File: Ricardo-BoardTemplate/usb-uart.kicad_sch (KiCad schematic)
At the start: 16 parts, among them J3 USB_C_Receptacle_USB2.0, U6 SC4216H/RT9059, U7 LTC4411

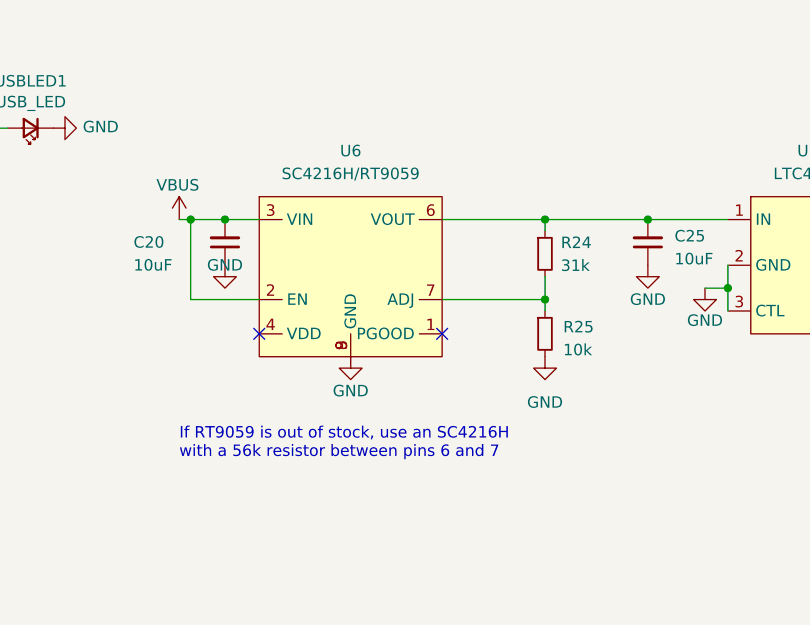
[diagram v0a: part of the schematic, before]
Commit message: most FP assignments to 0402
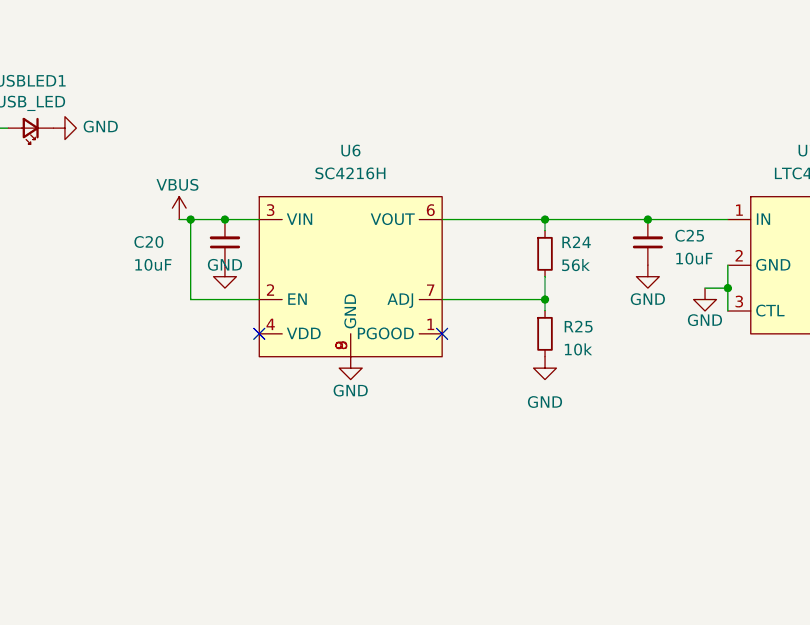
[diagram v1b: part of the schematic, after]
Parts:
- R15, R16, R18, R25: footprint Resistor_SMD:R_0603_1608Metric -> Resistor_SMD:R_0402_1005Metric
- R24: value 31k -> 56k; footprint Resistor_SMD:R_0603_1608Metric -> Resistor_SMD:R_0402_1005Metric
- U6: value SC4216H/RT9059 -> SC4216H
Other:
- note removed: "If RT9059 is out of stock, use an SC4216H with a 56k resistor between pins 6 and 7"
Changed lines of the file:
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@@
     (stroke (width 0) (type default) (color 0 0 0 0))
-  )
-  (text "If RT9059 is out of stock, use an SC4216H \nwith a 56k resistor between pins 6 and 7"
-    (at 179.07 129.54 0)
-    (effects (font (size 1.27 1.27)) (justify left bottom))
   )
   (label "Data+" (at 134.62 134.62 90)
@@
     (property "Reference" "R16" (id 0) (at 129.54 100.33 90))
     (property "Value" "5.1k" (id 1) (at 129.54 102.6414 90))
-    (property "Footprint" "Resistor_SMD:R_0603_1608Metric" (id 2) (at 123.19 99.06 0)
+    (property "Footprint" "Resistor_SMD:R_0402_1005Metric" (id 2) (at 123.19 99.06 0)
       (effects (font (size 1.27 1.27)) hide)
     )
@@
     (property "Reference" "R15" (id 0) (at 123.19 89.0016 90))
     (property "Value" "5.1k" (id 1) (at 123.19 91.313 90))
-    (property "Footprint" "Resistor_SMD:R_0603_1608Metric" (id 2) (at 123.19 93.98 0)
+    (property "Footprint" "Resistor_SMD:R_0402_1005Metric" (id 2) (at 123.19 93.98 0)
       (effects (font (size 1.27 1.27)) hide)
     )
@@
     (property "Reference" "R18" (id 0) (at 154.94 97.6884 90))
     (property "Value" "470" (id 1) (at 154.94 95.377 90))
-    (property "Footprint" "Resistor_SMD:R_0603_1608Metric" (id 2) (at 154.94 92.71 0)
+    (property "Footprint" "Resistor_SMD:R_0402_1005Metric" (id 2) (at 154.94 92.71 0)
       (effects (font (size 1.27 1.27)) hide)
     )
@@
       (effects (font (size 1.27 1.27)) (justify left))
     )
-    (property "Footprint" "Resistor_SMD:R_0603_1608Metric" (id 2) (at 219.71 115.57 0)
+    (property "Footprint" "Resistor_SMD:R_0402_1005Metric" (id 2) (at 219.71 115.57 0)
       (effects (font (size 1.27 1.27)) hide)
     )
@@
       (effects (font (size 1.27 1.27)) (justify left))
     )
-    (property "Value" "31k" (id 1) (at 221.4667 107.9905 0)
-      (effects (font (size 1.27 1.27)) (justify left))
-    )
-    (property "Footprint" "Resistor_SMD:R_0603_1608Metric" (id 2) (at 219.71 106.68 0)
+    (property "Value" "56k" (id 1) (at 221.4667 107.9905 0)
+      (effects (font (size 1.27 1.27)) (justify left))
+    )
+    (property "Footprint" "Resistor_SMD:R_0402_1005Metric" (id 2) (at 219.71 106.68 0)
       (effects (font (size 1.27 1.27)) hide)
     )
@@
     (in_bom yes) (on_board yes) (fields_autoplaced)
     (property "Reference" "U6" (id 0) (at 198.12 95.25 0))
-    (property "Value" "SC4216H/RT9059" (id 1) (at 198.12 97.79 0))
+    (property "Value" "SC4216H" (id 1) (at 198.12 97.79 0))
     (property "Footprint" "iclr:SOIC127P599X175-9N" (id 2) (at 198.12 96.52 0)
       (effects (font (size 1.27 1.27)) hide)

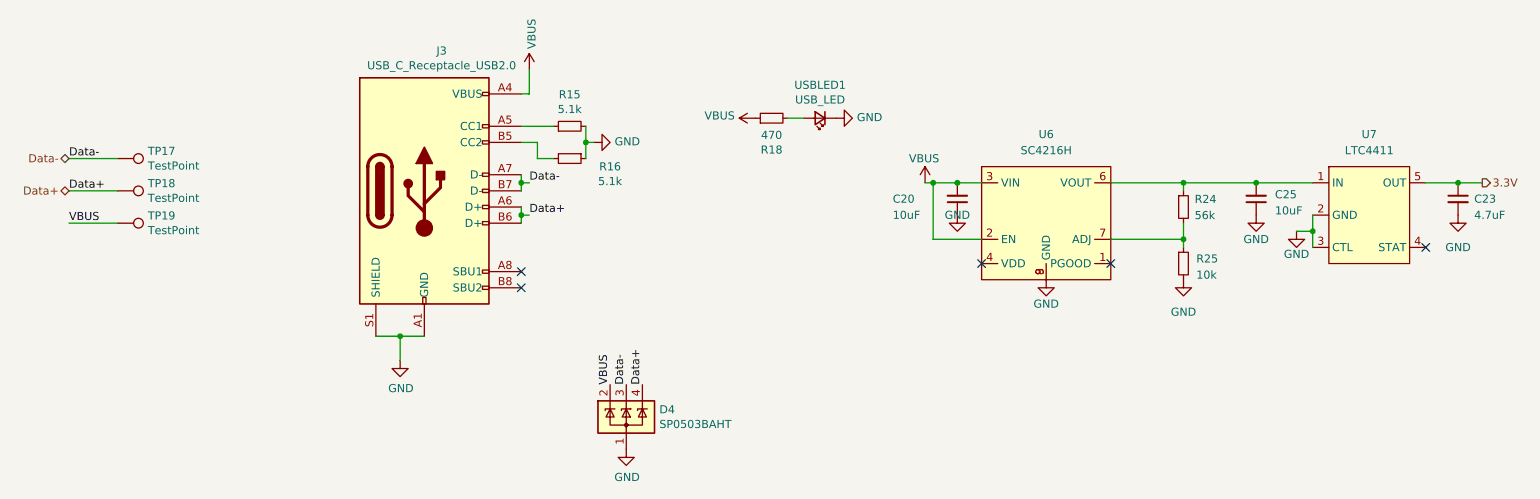
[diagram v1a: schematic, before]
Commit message: Initial buck boost layout
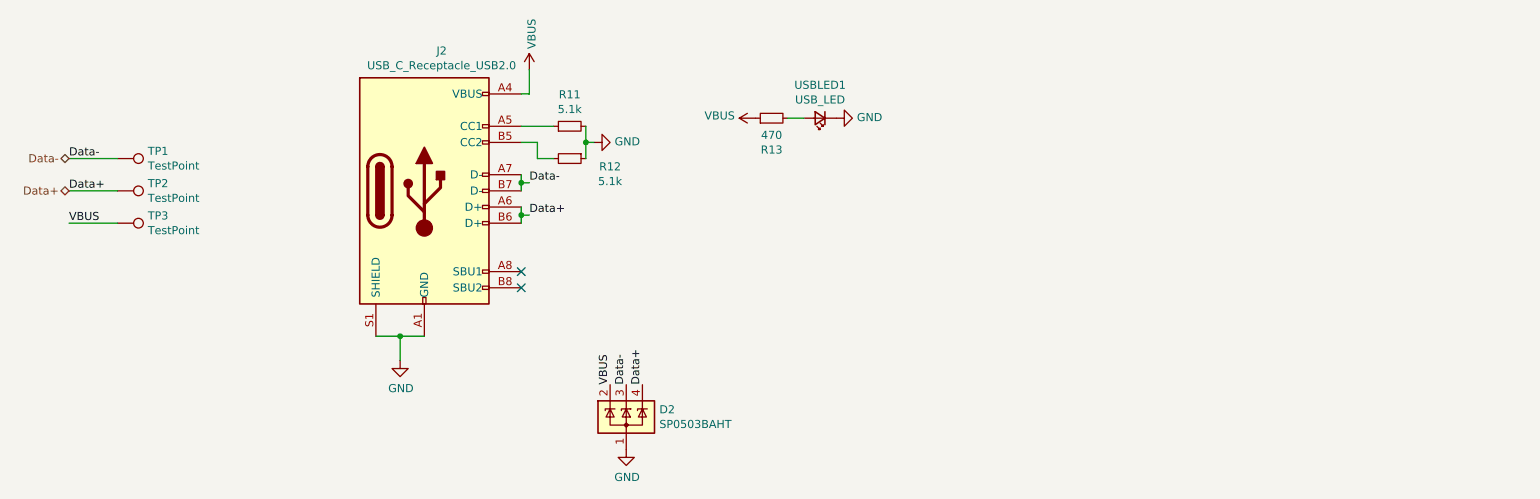
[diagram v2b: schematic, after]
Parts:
- removed C20, C25: 10uF, Capacitor_SMD:C_0603_1608Metric, symbol Device:C_Small
- removed C23: 4.7uF, Capacitor_SMD:C_0603_1608Metric, symbol Device:C_Small
- removed R24: 56k, Resistor_SMD:R_0402_1005Metric, symbol Device:R_Small
- removed R25: 10k, Resistor_SMD:R_0402_1005Metric, symbol Device:R_Small
- removed U6: SC4216H, iclr:SOIC127P599X175-9N, symbol iclr:RT9025-25GSP
- removed U7: LTC4411, Package_TO_SOT_SMD:SOT-23-5, symbol iclr:LTC4411
- USBLED1: footprint LED_SMD:LED_0603_1608Metric -> Resistor_SMD:R_0402_1005Metric
- renumbered D4 to D2, J3 to J2, R15 to R11, R16 to R12, R18 to R13, TP17 to TP1, TP18 to TP2, TP19 to TP3
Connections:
- no-connect marks 5 -> 2
